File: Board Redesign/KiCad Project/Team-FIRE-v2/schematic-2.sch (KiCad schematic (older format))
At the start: 20 parts, among them J4 Conn_01x03, J5 Conn_ARM_JTAG_SWD_10, U4 TXB0108DQSR, U7 TXB0104RUT

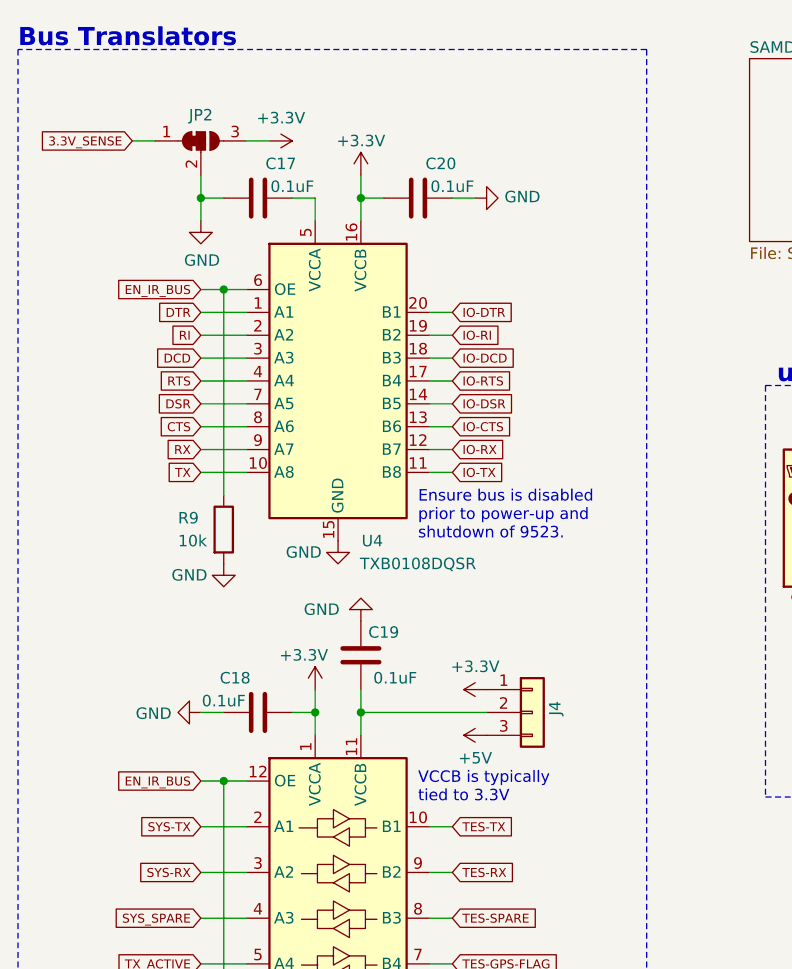
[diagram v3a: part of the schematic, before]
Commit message: Finished component selection for Bus Translators
- Finished filling out all details for every component in Bus Translator block
- Annotated existing schematic
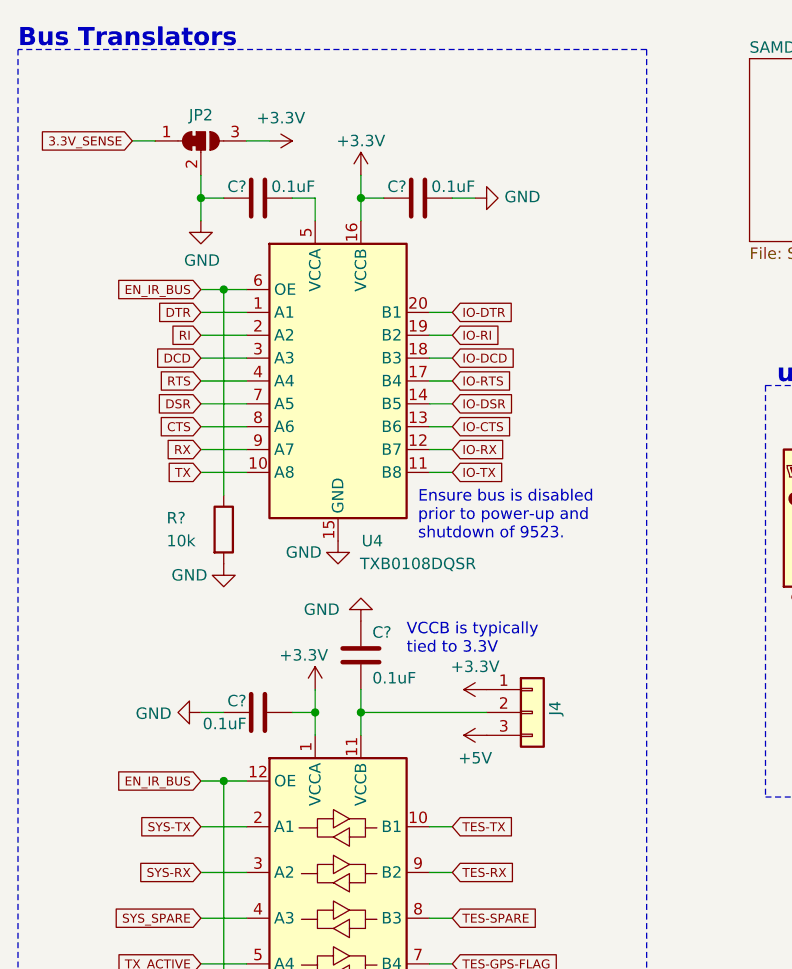
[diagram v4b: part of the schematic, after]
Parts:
- removed C17, C18, C19, C20: 0.1uF, Capacitor_SMD:C_0603_1608Metric, symbol Device:C
- removed R9: 10k, Resistor_SMD:R_0603_1608Metric, symbol Device:R
- added C? (x4): 0.1uF, Capacitor_SMD:C_0603_1608Metric, symbol Device:C
- added R?: 10k, Resistor_SMD:R_0603_1608Metric, symbol Device:R
- J4: Current Rating (none) -> 2 A; Description (none) -> PA6T voltage pin header; Link (none) -> https://www.digikey.com/product-detail/en/jst-sales-america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; Manufacturer (none) -> JST Sales America Inc.; Supplier (none) -> Digikey; Supplier PN (none) -> 455-1750-1-ND; Voltage Rating (none) -> 100 V
- R10: Link (none) -> https://www.mouser.com/ProductDetail/Vishay-Beyschlag/MCT06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; MPN (none) -> MCT06030E1002BP100; Manufacturer (none) -> Vishay; Supplier (none) -> Mouser; Supplier PN (none) -> 594-MCT06030E1002BP1; Tolerance (none) -> 0.1%; Type (none) -> Thin Film Resistor; Voltage Rating (none) -> 75 V
- U4: Description (none) -> Voltage bus shifter; Link (none) -> https://www.mouser.com/ProductDetail/Texas-Instruments/TXB0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; Manufacturer (none) -> Texas Instruments; Supplier (none) -> Mouser; Supplier PN (none) -> 595-TXB0108DQSR; Voltage Rating (none) -> 1.2/1.65 V to 5.5 V
- U7: Description (none) -> 5V or 3V voltage shifter; Link (none) -> https://www.mouser.com/ProductDetail/Texas-Instruments/TXB0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; MPN (none) -> TXB0104RUTR; Manufacturer (none) -> Texas Instruments; Supplier (none) -> Mouser; Supplier PN (none) -> 595-TXB0104RUTR; Voltage Rating (none) -> 1.2/1.65 V to 5.5 V
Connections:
- net +3V3: now also C?.1, C?.2
- net EN_IR_BUS: now also R?.1
- net GND: now also C?.1, C?.1, C?.1, C?.2, R?.2
- net at U4.5 (VCCA): now also C?.2
- net at J4.2 (Pin_2), U7.11 (VCCB): now also C?.2

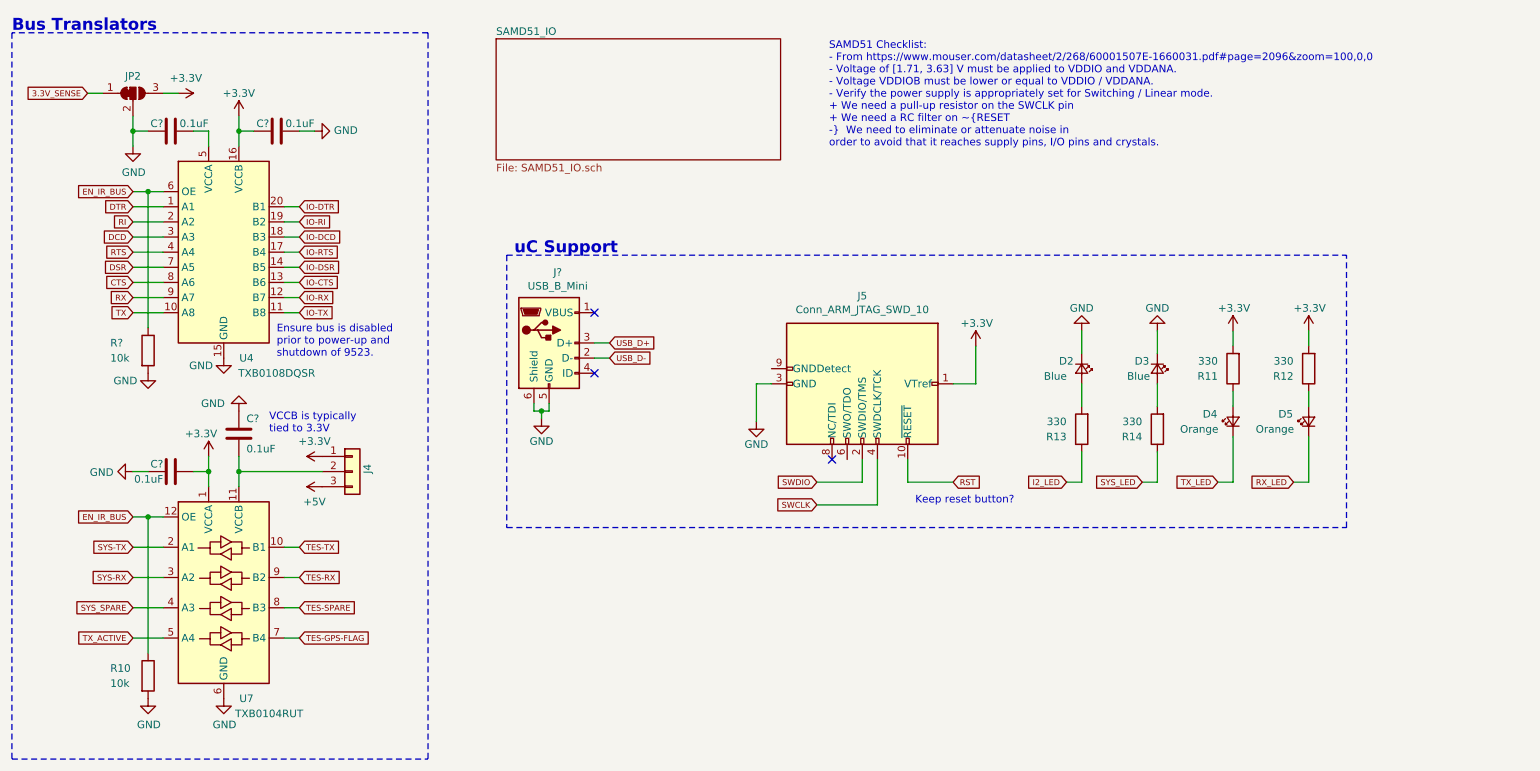
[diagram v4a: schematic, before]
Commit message: Made a lot of changes...
- Added symbol, footprint for Micro USB B connector
- Fixed Flash Memory schematic
- Added details for many components
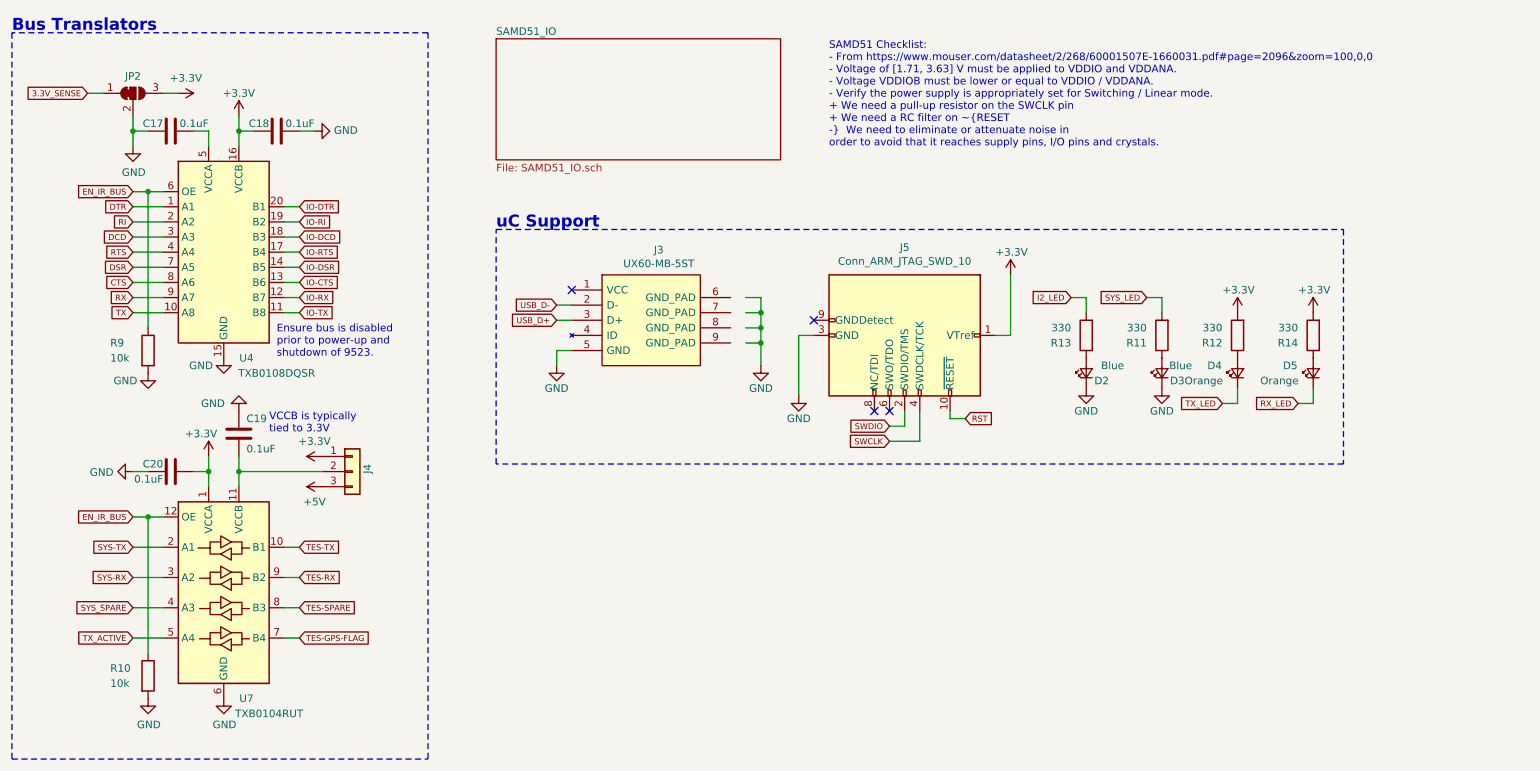
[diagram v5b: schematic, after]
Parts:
- removed J?: USB_B_Mini, symbol Connector:USB_B_Mini
- added J3: UX60-MB-5ST, Team-FIRE:HIROSE-UX60-MB-5ST, symbol Team-FIRE:UX60-MB-5ST
- R11, R12, R13, R14: Link (none) -> https://www.mouser.com/ProductDetail/Yageo/SR0603FR-7T330RL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; MPN (none) -> SR0603FR-7T330RL; Manufacturer (none) -> Yageo; Supplier (none) -> Mouser; Supplier PN (none) -> 603-SR0603FR-7T330RL; Tolerance (none) -> 1%; Type (none) -> Thick Film Resistor; Voltage Rating (none) -> 75 V
- gave numbers to parts that had none: 5
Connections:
- wire segments 81 -> 78
- no-connect marks 3 -> 4
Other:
- note removed: "Keep reset button?"
- moved on the sheet: D2, D3, D4, D5, R13

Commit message: fixed issue
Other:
- moved on the sheet: J3
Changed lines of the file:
@@
 Text Notes 3800 2000 0    79   ~ 16
 uC Support
-Text GLabel 4200 2600 0    39   Input ~ 0
+Text GLabel 4200 2750 0    39   Input ~ 0
 USB_D+
 $Comp
@@
 U 1 1 5EB2EB4B
 P 6500 2700
-F 0 "J5" V 5919 2700 50  0000 C CNN
-F 1 "Conn_ARM_JTAG_SWD_10" V 6010 2700 50  0000 C CNN
+F 0 "J5" V 6050 2700 50  0000 C CNN
+F 1 "Conn_ARM_JTAG_SWD_10" V 6010 2700 50  0001 C CNN
 F 2 "" H 6500 2700 50  0001 C CNN
 F 3 "http://infocenter.arm.com/help/topic/com.arm.doc.ddi0314h/DDI0314H_coresight_components_trm.pdf" V 6150 1450 50  0001 C CNN
@@
 L Team-FIRE:UX60-MB-5ST J3
 U 1 1 5EB793C5
-P 4300 2400
-F 0 "J3" H 4875 2665 50  0000 C CNN
-F 1 "UX60-MB-5ST" H 4875 2574 50  0000 C CNN
-F 2 "Team-FIRE:HIROSE-UX60-MB-5ST" H 5550 2500 50  0001 L CNN
-F 3 "http://www.farnell.com/datasheets/1824852.pdf" H 5550 2400 50  0001 L CNN
-F 4 "Hirose" H 5550 2100 50  0001 L CNN "Manufacturer"
-F 5 "UX60-MB-5ST" H 5550 2000 50  0001 L CNN "MPN"
-F 6 "798-UX60-MB-5ST" H 5550 1900 50  0001 L CNN "Supplier PN"
-F 7 "https://www.mouser.com/ProductDetail/Hirose-Connector/UX60-MB-5ST?qs=sGAEpiMZZMulM8LPOQ%252BykzmHhzPuOAFGIpscEVPIFWo%3D" H 4300 2400 50  0001 C CNN "Link"
-F 8 "1 A" H 4300 2400 50  0001 C CNN "Current Rating"
-F 9 "USB B Mini Connector" H 4300 2400 50  0001 C CNN "Description"
-F 10 "Mouser" H 5550 1600 50  0001 L CNN "Supplier"
-	1    4300 2400
-	1    0    0    -1
-$EndComp
-NoConn ~ 4300 2400
-Text GLabel 4200 2500 0    39   Input ~ 0
+P 4300 2550
+F 0 "J3" H 4875 2815 50  0000 C CNN
+F 1 "UX60-MB-5ST" H 4875 2724 50  0000 C CNN
+F 2 "Team-FIRE:HIROSE-UX60-MB-5ST" H 5550 2650 50  0001 L CNN
+F 3 "http://www.farnell.com/datasheets/1824852.pdf" H 5550 2550 50  0001 L CNN
+F 4 "Hirose" H 5550 2250 50  0001 L CNN "Manufacturer"
+F 5 "UX60-MB-5ST" H 5550 2150 50  0001 L CNN "MPN"
+F 6 "798-UX60-MB-5ST" H 5550 2050 50  0001 L CNN "Supplier PN"
+F 7 "https://www.mouser.com/ProductDetail/Hirose-Connector/UX60-MB-5ST?qs=sGAEpiMZZMulM8LPOQ%252BykzmHhzPuOAFGIpscEVPIFWo%3D" H 4300 2550 50  0001 C CNN "Link"
+F 8 "1 A" H 4300 2550 50  0001 C CNN "Current Rating"
+F 9 "USB B Mini Connector" H 4300 2550 50  0001 C CNN "Description"
+F 10 "Mouser" H 5550 1750 50  0001 L CNN "Supplier"
+	1    4300 2550
+	1    0    0    -1
+$EndComp
+NoConn ~ 4300 2550
+Text GLabel 4200 2650 0    39   Input ~ 0
 USB_D-
 Wire Wire Line
-	4300 2500 4200 2500
-Wire Wire Line
-	4200 2600 4300 2600
-Wire Wire Line
-	4300 2800 4200 2800
-Wire Wire Line
-	4200 2800 4200 2900
-Wire Wire Line
-	5550 2450 5450 2450
-Wire Wire Line
-	5550 2900 5550 2750
-Wire Wire Line
-	5450 2550 5550 2550
-Connection ~ 5550 2550
-Wire Wire Line
-	5550 2550 5550 2450
-Wire Wire Line
-	5450 2650 5550 2650
-Connection ~ 5550 2650
-Wire Wire Line
-	5550 2650 5550 2550
-Wire Wire Line
-	5450 2750 5550 2750
-Connection ~ 5550 2750
-Wire Wire Line
-	5550 2750 5550 2650
+	4300 2650 4200 2650
+Wire Wire Line
+	4200 2750 4300 2750
+Wire Wire Line
+	4300 2950 4200 2950
+Wire Wire Line
+	4200 2950 4200 3050
+Wire Wire Line
+	5550 2600 5450 2600
+Wire Wire Line
+	5550 3050 5550 2900
+Wire Wire Line
+	5450 2700 5550 2700
+Connection ~ 5550 2700
+Wire Wire Line
+	5550 2700 5550 2600
+Wire Wire Line
+	5450 2800 5550 2800
+Connection ~ 5550 2800
+Wire Wire Line
+	5550 2800 5550 2700
+Wire Wire Line
+	5450 2900 5550 2900
+Connection ~ 5550 2900
+Wire Wire Line
+	5550 2900 5550 2800
 $Comp
 L power:GND #PWR010
 U 1 1 5EB94E46
-P 4200 2900
-F 0 "#PWR010" H 4200 2650 50  0001 C CNN
-F 1 "GND" H 4200 2750 50  0000 C CNN
-F 2 "" H 4200 2900 50  0001 C CNN
-F 3 "" H 4200 2900 50  0001 C CNN
-	1    4200 2900
+P 4200 3050
+F 0 "#PWR010" H 4200 2800 50  0001 C CNN
+F 1 "GND" H 4200 2900 50  0000 C CNN
+F 2 "" H 4200 3050 50  0001 C CNN
+F 3 "" H 4200 3050 50  0001 C CNN
+	1    4200 3050
 	1    0    0    -1
 $EndComp
@@
 L power:GND #PWR012
 U 1 1 5EB95383
-P 5550 2900
-F 0 "#PWR012" H 5550 2650 50  0001 C CNN
-F 1 "GND" H 5550 2750 50  0000 C CNN
-F 2 "" H 5550 2900 50  0001 C CNN
-F 3 "" H 5550 2900 50  0001 C CNN
-	1    5550 2900
-	1    0    0    -1
-$EndComp
+P 5550 3050
+F 0 "#PWR012" H 5550 2800 50  0001 C CNN
+F 1 "GND" H 5550 2900 50  0000 C CNN
+F 2 "" H 5550 3050 50  0001 C CNN
+F 3 "" H 5550 3050 50  0001 C CNN
+	1    5550 3050
+	1    0    0    -1
+$EndComp

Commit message: Fixed some stuff (woops)
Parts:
- removed J3: UX60-MB-5ST, Team-FIRE:HIROSE-UX60-MB-5ST, symbol Team-FIRE:UX60-MB-5ST
- added J?: UX60-MB-5ST, Team-FIRE:HIROSE-UX60-MB-5ST, symbol Team-FIRE:UX60-MB-5ST
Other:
- moved on the sheet: D2, D3, D4, D5, J5, R11, R12, R13, R14
